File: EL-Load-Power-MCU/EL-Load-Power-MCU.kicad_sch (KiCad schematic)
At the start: 69 parts, among them J1 Conn_01x02, J10 Power for serial interface, J11 Conn_02x08_Odd_Even, J2 Screw_Terminal_01x02, J3 Touchscreen, J4 JST-S6B-PH-SM4, J7 Conn_02x08_Odd_Even, J8 Conn_02x06_Odd_Even, T1 Wuerth_750316031, T2 Wuerth_750316031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

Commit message: Did #7, #10 and few items from #2
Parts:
- removed J2: Screw_Terminal_01x02, TerminalBlock_Phoenix:TerminalBlock_Phoenix_PT-1,5-2-5.0-H_1x02_P5.00mm_Horizontal, symbol Connector:Screw_Terminal_01x02
- removed JP8: Jumper_2_Bridged, Connector_PinHeader_2.54mm:PinHeader_1x02_P2.54mm_Vertical, symbol Jumper:Jumper_2_Bridged
- added J2: Conn_01x02, Connector_Phoenix_MC:PhoenixContact_MCV_1,5_2-G-3.81_1x02_P3.81mm_Vertical, symbol Connector_Generic:Conn_01x02
- added JP10: Select 5V source, Connector_PinHeader_2.54mm:PinHeader_1x03_P2.54mm_Vertical, symbol Jumper:Jumper_3_Open
- added JP8: Select Fan Voltage, Connector_PinHeader_2.54mm:PinHeader_1x03_P2.54mm_Vertical, symbol Jumper:Jumper_3_Open
- added JP9: Jumper_2_Bridged, Connector_PinHeader_2.54mm:PinHeader_1x02_P2.54mm_Vertical, symbol Jumper:Jumper_2_Bridged
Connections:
- net +3V3: now also J7.14 (Pin_14)
- net +5V_ISO: now also JP10.2 (C), JP8.1 (A); no longer L1.4
- net GND: no longer J7.14 (Pin_14)
- net GND_ISO: now also J2.2 (Pin_2)
- net +5V_FANS renamed +V_FANS
- net +V_FANS: now also JP8.2 (C)
- new net: JP10.1 (A), L1.4
- new net +12V_ISO: J2.1 (Pin_1), JP8.3 (B), JP9.2 (B)
- new net Standalone Power/12Vin: JP9.1 (A)
- new net Standalone Power/5Vout: JP10.3 (B)
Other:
- added sheet Standalone Power (untitled.kicad_sch)
- note added: "Standalone only, not for BB3 module"
- moved on the sheet: D6, J1, L1, R4

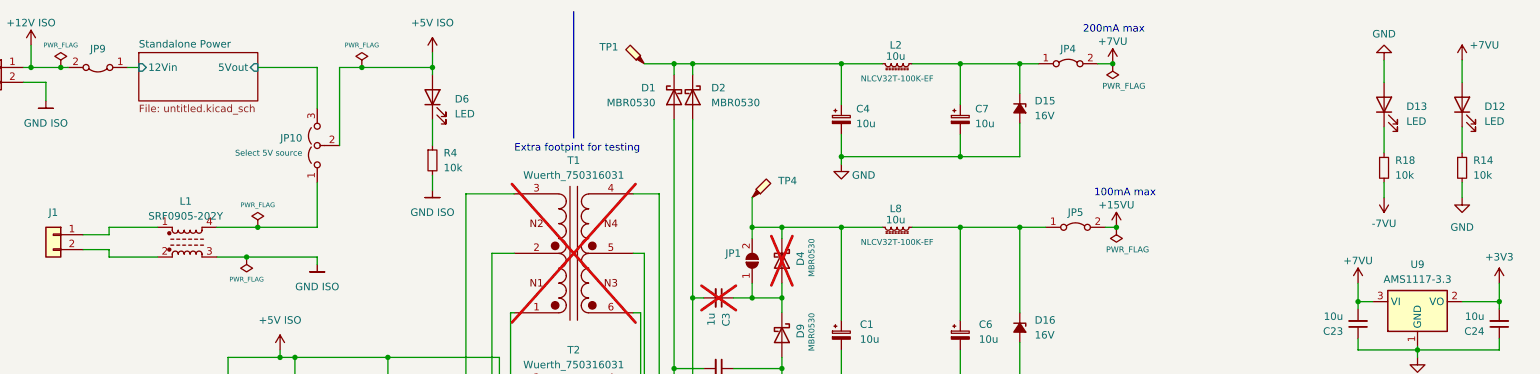
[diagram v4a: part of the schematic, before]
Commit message: Added +15VU led, fixed JP1
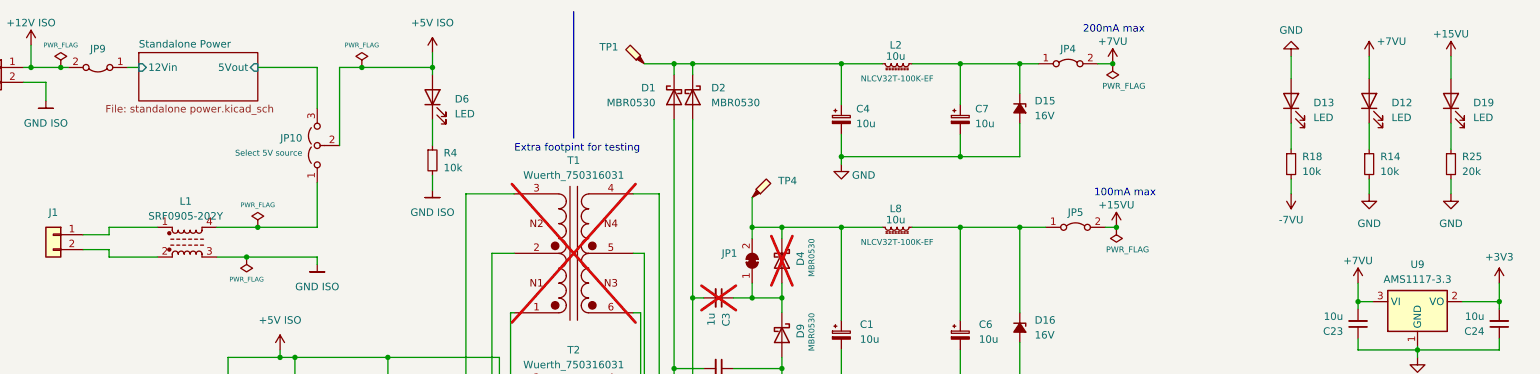
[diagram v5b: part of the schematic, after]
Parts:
- removed JP1: SolderJumper_2_Open, Jumper:SolderJumper-2_P1.3mm_Open_RoundedPad1.0x1.5mm, symbol Jumper:SolderJumper_2_Open
- added D19: LED, LED_SMD:LED_0805_2012Metric, symbol Device:LED
- added JP1: SolderJumper_2_Bridged, Jumper:SolderJumper-2_P1.3mm_Bridged2Bar_RoundedPad1.0x1.5mm, symbol Jumper:SolderJumper_2_Bridged
- added R25: 20k, Resistor_SMD:R_0805_2012Metric, symbol Device:R_Small
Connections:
- net +15VU: now also D19.2 (A)
- net GND: now also R25.2
- net at C1.1, D4.1 (K), L8.2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: now also JP1.2 (B)
- net at C3.1, D4.2 (A), D9.1 (K): now also JP1.1 (A)
- new net: D19.1 (K), R25.1
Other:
- sheet Standalone Power: file untitled.kicad_sch -> standalone power.kicad_sch
- moved on the sheet: D12, D13, R14, R18

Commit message: Working on #4,#2 fixed #8,#22
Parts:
- D16: value 16V -> 20V; Part_Name D_Z_16V_miniMELF -> D_Z_20V_miniMELF
- T1: value Wuerth_750316031 -> Wuerth_750315371
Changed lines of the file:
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@@
       (effects (font (size 1.27 1.27)))
     )
-    (property "Value" "Wuerth_750316031" (at 116.205 41.91 0)
+    (property "Value" "Wuerth_750315371" (at 116.205 41.91 0)
       (effects (font (size 1.27 1.27)))
     )
@@
   (symbol (lib_id "Device:D_Zener_Small_Filled") (at 192.405 67.945 270) (unit 1)
     (in_bom yes) (on_board yes) (dnp no) (fields_autoplaced)
-    (property "Reference" "D16" (at 194.945 66.675 90)
-      (effects (font (size 1.27 1.27)) (justify left))
-    )
-    (property "Value" "16V" (at 194.945 69.215 90)
+    (property "Reference" "D16" (at 194.31 66.675 90)
+      (effects (font (size 1.27 1.27)) (justify left))
+    )
+    (property "Value" "20V" (at 194.31 69.215 90)
       (effects (font (size 1.27 1.27)) (justify left))
     )
@@
       (effects (font (size 1.27 1.27)))
     )
-    (property "Part_Name" "D_Z_16V_miniMELF " (at 192.405 67.945 0)
-      (effects (font (size 1.27 1.27)) hide)
-    )
+    (property "Part_Name" "D_Z_20V_miniMELF" (at 192.405 67.945 0)
+      (effects (font (size 1.27 1.27)) hide)
+    )

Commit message: EL-Load-Power-MCU PCB v4r4 release.
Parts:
- removed J3: Touchscreen, Connector_PinSocket_2.54mm:PinSocket_1x11_P2.54mm_Vertical, symbol Connector:Conn_01x11_Pin
- removed J4: JST-S6B-PH-SM4, Connector_JST:JST_PH_S6B-PH-SM4-TB_1x06-1MP_P2.00mm_Horizontal, symbol Connector:Conn_01x06_Pin
- added C29: 1u, Capacitor_SMD:C_0805_2012Metric, symbol Device:C_Small
- added C31: 100n, Capacitor_SMD:C_0805_2012Metric, symbol Device:C_Small
- added C32: 10u, Capacitor_SMD:CP_Elec_5x5.8, symbol Device:C_Polarized_Small
- added JP11: HW V3/V4, Connector_PinHeader_2.54mm:PinHeader_1x02_P2.54mm_Vertical, symbol Jumper:Jumper_2_Open
- C1, C13, C19, C30, C4, C6, C7: footprint Capacitor_SMD:CP_Elec_6.3x5.8 -> Capacitor_SMD:CP_Elec_5x5.8; Part_Name C_47u_35V_Elec_6.3_20% -> C_10uF_50V_Elec_5
- C16, C17, C21: Part_Name C_100.0nF_50V_0805_10% -> C_100.0nF_50V_0805_10%_X7R
- C18, C20, C22, C23: footprint Capacitor_SMD:C_0805_2012Metric -> Capacitor_SMD:CP_Elec_5x5.8; symbol Device:C_Small -> Device:C_Polarized_Small; Part_Name C_10.0uF_6V3_X7R_10%_0805 -> C_10uF_50V_Elec_5
- J11: value Conn_02x08_Odd_Even -> IDC-Header 2x08 P2.54mm
- J7: value Conn_02x08_Odd_Even -> PinHeader 2x08 P2.54mm; footprint Connector_PinSocket_2.54mm:PinSocket_2x08_P2.54mm_Vertical -> Connector_PinHeader_2.54mm:PinHeader_2x08_P2.54mm_Vertical
- J8: value Conn_02x06_Odd_Even -> PinHeader 2x08 P2.54mm
- JP10, JP8: Consumable (none) -> 1; Part_Name (none) -> H_Male_1x40_vertical_THT
- TP5: value GND -> TestPoint_Probe
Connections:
- net MCU/EL-DAC_RDY is gone; now on net MCU/EL-ADC_CS: J7.6 (Pin_6)
- net +12V_ISO: now also L1.3; no longer J2.1 (Pin_1)
- net +15VU: no longer J8.8 (Pin_8)
- net +3V3: now also J7.13 (Pin_13), C29.1, C31.2, C32.1; no longer J7.14 (Pin_14)
- net +5VD: now also C22.1; no longer C22.2
- net +7VU: now also C20.1, C23.1; no longer C20.2, C23.2
- net +V_FANS: now also C18.1; no longer C18.2
- net GND: now also C20.2, C22.2, C23.2, J7.11 (Pin_11), C29.2, C31.1, C32.2; no longer C20.1, C22.1, C23.1, J7.12 (Pin_12)
- net GND_ISO: now also C18.2, J1.2 (Pin_2), L1.4; no longer C18.1, J2.2 (Pin_2), L1.3
- net MCU/EL-ADC_CLK: now also J7.9 (Pin_9); no longer J7.10 (Pin_10)
- net MCU/EL-ADC_CS: no longer J7.5 (Pin_5)
- net MCU/EL-DAC1_CS: now also J7.12 (Pin_12); no longer J7.11 (Pin_11)
- net MCU/EL-DAC2_CS: now also J7.15 (Pin_15); no longer J7.16 (Pin_16)
- net MCU/EL-SPI_RX: now also J7.10 (Pin_10); no longer J7.9 (Pin_9)
- net MCU/EL-SPI_SCK: now also J7.8 (Pin_8); no longer J7.7 (Pin_7)
- net MCU/EL-SPI_TX: now also J7.7 (Pin_7); no longer J7.8 (Pin_8)
- net MCU/OCPtriggered: now also J7.2 (Pin_2); no longer J7.1 (Pin_1)
- net MCU/OVPtriggered: now also J7.4 (Pin_4); no longer J7.3 (Pin_3)
- net MCU/clampOff: now also J7.3 (Pin_3); no longer J7.4 (Pin_4)
- net MCU/currRangeLow: now also J7.14 (Pin_14); no longer J7.13 (Pin_13)
- net MCU/resetProt: now also J7.1 (Pin_1); no longer J7.2 (Pin_2)
- net MCU/~{Von}: now also J7.16 (Pin_16); no longer J7.15 (Pin_15)
- net at J1.1 (Pin_1): now also JP10.1 (A); no longer L1.1
- net at L1.2: now also J2.1 (Pin_1); no longer J1.2 (Pin_2)
- net SCL renamed MCU/HWIO_SCL
- net MCU/HWIO_SCL: no longer J11.13 (Pin_13)
- net SDA renamed MCU/HWIO_SDA
- net MCU/HWIO_SDA: no longer J11.12 (Pin_12)
- new net: J2.2 (Pin_2), L1.1
- new net MCU/EL-ADC_RDY: J7.5 (Pin_5)
- new net MCU/reversePolarity: JP11.2 (B)
- new net _KEYS_SCL: J11.13 (Pin_13)
- new net _KEYS_SDA: J11.12 (Pin_12)
- new net _reversePolarity: J8.8 (Pin_8), JP11.1 (A)
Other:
- sheet MCU ports: added EL-ADC_RDY, HWIO_SCL, HWIO_SDA, KEYS_SCL, KEYS_SDA, reversePolarity; removed EL-DAC_RDY, SCL, SDA
- note removed: "I2C address: 0x20"
- note removed: "Keypad"
- note removed: "from pico"
- moved on the sheet: D6, J1, J2, JP10, JP9, L1, R4
